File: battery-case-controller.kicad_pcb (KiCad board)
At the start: 6 copper layers, 109 x 55 mm, 187 parts, among them J31 +, J32 DISPLAY, J33 A, J34 HALL, J35 B, J36 MOT_AUX, J37 C, J38 CRANK, J39 GND, J40 CAN_IN, J41 CAN_OUT, J42 Debug, J43 SWD, M31 MountingHole_Pad, M32 MountingHole_Pad, M33 MountingHole_Pad, Q31 BSC040N08, Q32 BSC040N08, Q33 BSC040N08, Q34 BSC040N08, Q35 BSC040N08, Q36 BSC040N08, Q37 BSC040N08, Q38 BSC040N08, Q39 BSC040N08, Q40 BSC040N08, Q41 BSC040N08, Q42 BSC040N08, U31 Enable, U32 LM5109B, U33 INA240A2PWR, U34 LM5109B, U35 INA240A2PWR, U36 LM5109B, U37 INA240A2PWR, U38 LM5008, U39 XC6206P332MR, U40 XC6206P332MR, U41 LMR12010X, U42 SN65HVD230, U43 STM32G491CxT, X31 8MHz

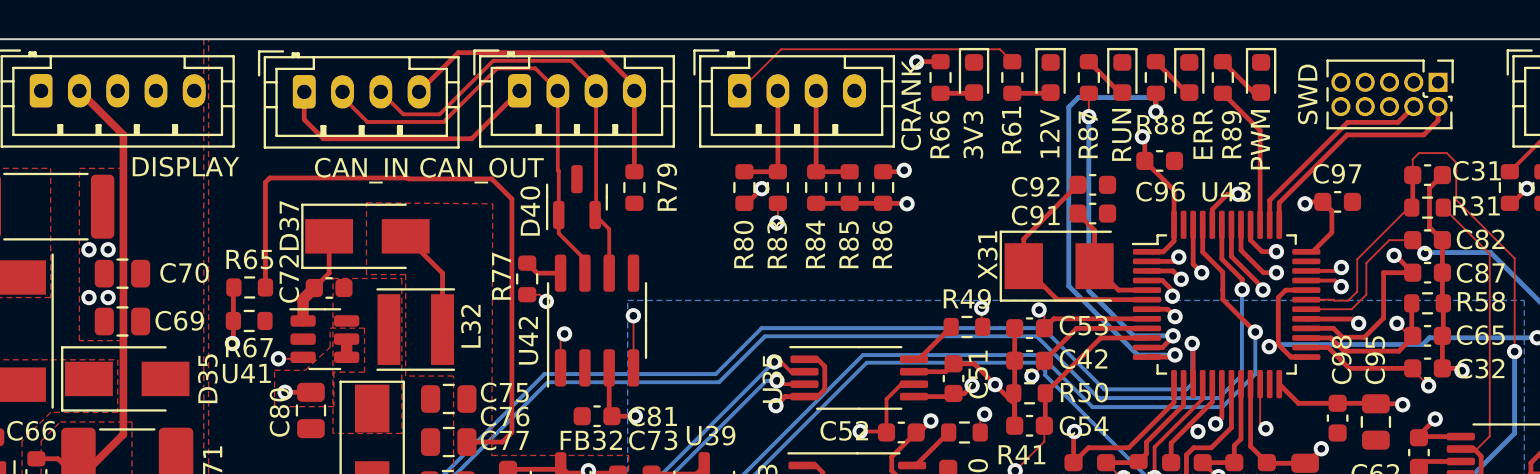
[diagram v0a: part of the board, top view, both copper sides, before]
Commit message: Fixed pinning error for Display RX and PWM Break
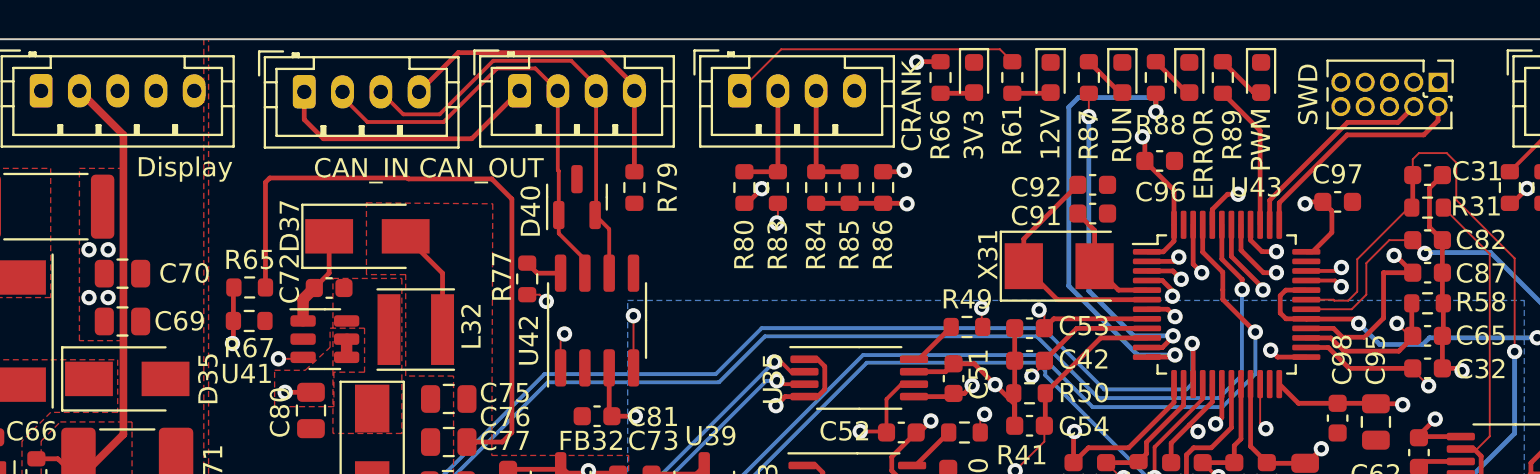
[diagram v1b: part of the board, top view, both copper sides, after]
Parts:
- D42: value ERR -> ERROR
- J32: value DISPLAY -> Display
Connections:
- U43 pad 25: /Interface/PWM_BREAK -> /mcu/DISP_RX
- U43 pad 29: /mcu/DISP_RX -> /Interface/PWM_BREAK
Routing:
- net /mcu/DISP_RX: track 74.1 -> 69.6 mm
- net /Interface/PWM_BREAK: track 27.7 -> 23.8 mm
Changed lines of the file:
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@@
   (net 99 "unconnected-(J43-Pad8)")
   (net 100 "unconnected-(J43-Pad9)")
-  (net 101 "Net-(U33-Pad8)")
+  (net 101 "Net-(R41-Pad1)")
   (net 102 "Net-(R43-Pad2)")
   (net 103 "Net-(R46-Pad2)")
-  (net 104 "Net-(U35-Pad8)")
+  (net 104 "Net-(R49-Pad1)")
   (net 105 "Net-(R51-Pad2)")
   (net 106 "Net-(R54-Pad2)")
-  (net 107 "Net-(U37-Pad8)")
+  (net 107 "Net-(R57-Pad1)")
   (net 108 "Net-(R59-Pad1)")
   (net 109 "Net-(R63-Pad2)")
@@
       (net 2 "GNDA") (pinfunction "REF1") (pintype "passive"))
     (pad "8" smd roundrect (at 2.8625 -0.975 180) (size 1.475 0.4) (layers "F.Cu" "F.Paste" "F.Mask") (roundrect_rratio 0.25)
-      (net 107 "Net-(U37-Pad8)") (pintype "output"))
+      (net 107 "Net-(R57-Pad1)") (pintype "output"))
     (model "${KICAD6_3DMODEL_DIR}/Package_SO.3dshapes/TSSOP-8_4.4x3mm_P0.65mm.wrl"
       (offset (xyz 0 0 0))
@@
       (effects (font (size 1 1) (thickness 0.15)))
     )
-    (fp_text value "DISPLAY" (at 7.5 4) (layer "F.SilkS")
+    (fp_text value "Display" (at 7.5 4) (layer "F.SilkS")
       (effects (font (size 1 1) (thickness 0.15)))
     )
@@
       (net 2 "GNDA") (pinfunction "REF1") (pintype "passive"))
     (pad "8" smd roundrect (at 2.8625 -0.975) (size 1.475 0.4) (layers "F.Cu" "F.Paste" "F.Mask") (roundrect_rratio 0.25)
-      (net 104 "Net-(U35-Pad8)") (pintype "output"))
+      (net 104 "Net-(R49-Pad1)") (pintype "output"))
     (model "${KICAD6_3DMODEL_DIR}/Package_SO.3dshapes/TSSOP-8_4.4x3mm_P0.65mm.wrl"
       (offset (xyz 0 0 0))
@@
     (fp_line (start -0.8 0.4125) (end -0.8 -0.4125) (layer "F.Fab") (width 0.1))
     (pad "1" smd roundrect (at -0.825 0) (size 0.8 0.95) (layers "F.Cu" "F.Paste" "F.Mask") (roundrect_rratio 0.25)
-      (net 104 "Net-(U35-Pad8)") (pintype "passive"))
+      (net 104 "Net-(R49-Pad1)") (pintype "passive"))
     (pad "2" smd roundrect (at 0.825 0) (size 0.8 0.95) (layers "F.Cu" "F.Paste" "F.Mask") (roundrect_rratio 0.25)
       (net 50 "/mcu/AIN_IA") (pintype "passive"))
@@
       (net 2 "GNDA") (pinfunction "REF1") (pintype "passive"))
     (pad "8" smd roundrect (at 2.8625 -0.975) (size 1.475 0.4) (layers "F.Cu" "F.Paste" "F.Mask") (roundrect_rratio 0.25)
-      (net 101 "Net-(U33-Pad8)") (pintype "output"))
+      (net 101 "Net-(R41-Pad1)") (pintype "output"))
     (model "${KICAD6_3DMODEL_DIR}/Package_SO.3dshapes/TSSOP-8_4.4x3mm_P0.65mm.wrl"
       (offset (xyz 0 0 0))
@@
     (fp_line (start -0.8 0.4125) (end -0.8 -0.4125) (layer "F.Fab") (width 0.1))
     (pad "1" smd roundrect (at -0.825 0) (size 0.8 0.95) (layers "F.Cu" "F.Paste" "F.Mask") (roundrect_rratio 0.25)
-      (net 101 "Net-(U33-Pad8)") (pintype "passive"))
+      (net 101 "Net-(R41-Pad1)") (pintype "passive"))
     (pad "2" smd roundrect (at 0.825 0) (size 0.8 0.95) (layers "F.Cu" "F.Paste" "F.Mask") (roundrect_rratio 0.25)
       (net 47 "/mcu/AIN_IB") (pintype "passive"))
@@
     (property "Sheetname" "mcu")
     (attr smd)
-    (fp_text reference "U43" (at 0 -5.85) (layer "F.SilkS")
+    (fp_text reference "U43" (at 1.55 -6.11) (layer "F.SilkS")
       (effects (font (size 1 1) (thickness 0.15)))
     )
@@
       (net 14 "+3V3") (pinfunction "VDD") (pintype "power_in"))
     (pad "25" smd roundrect (at 4.1625 2.75) (size 1.475 0.3) (layers "F.Cu" "F.Paste" "F.Mask") (roundrect_rratio 0.25)
-      (net 43 "/Interface/PWM_BREAK") (pinfunction "PB11") (pintype "bidirectional"))
+      (net 25 "/mcu/DISP_RX") (pinfunction "PB11") (pintype "bidirectional"))
     (pad "26" smd roundrect (at 4.1625 2.25) (size 1.475 0.3) (layers "F.Cu" "F.Paste" "F.Mask") (roundrect_rratio 0.25)
       (net 3 "/mcu/AIN_VDC") (pinfunction "PB12") (pintype "bidirectional"))
@@
       (net 18 "/Interface/TORQ_CRK") (pinfunction "PB14") (pintype "bidirectional"))
     (pad "29" smd roundrect (at 4.1625 0.75) (size 1.475 0.3) (layers "F.Cu" "F.Paste" "F.Mask") (roundrect_rratio 0.25)
-      (net 25 "/mcu/DISP_RX") (pinfunction "PB15") (pintype "bidirectional"))
+      (net 43 "/Interface/PWM_BREAK") (pinfunction "PB15") (pintype "bidirectional"))
     (pad "30" smd roundrect (at 4.1625 0.25) (size 1.475 0.3) (layers "F.Cu" "F.Paste" "F.Mask") (roundrect_rratio 0.25)
       (net 15 "/Interface/TEMP_MOT") (pinfunction "PA8") (pintype "bidirectional"))
@@
       (effects (font (size 1 1) (thickness 0.15)))
     )
-    (fp_text value "ERR" (at 3 -0.75 90) (layer "F.SilkS")
+    (fp_text value "ERROR" (at 4 -0.75 90) (layer "F.SilkS")
       (effects (font (size 1 1) (thickness 0.15)))
     )
@@
     (fp_line (start 0.8 0.4125) (end -0.8 0.4125) (layer "F.Fab") (width 0.1))
     (pad "1" smd roundrect (at -0.825 0 180) (size 0.8 0.95) (layers "F.Cu" "F.Paste" "F.Mask") (roundrect_rratio 0.25)
-      (net 107 "Net-(U37-Pad8)") (pintype "passive"))
+      (net 107 "Net-(R57-Pad1)") (pintype "passive"))
     (pad "2" smd roundrect (at 0.825 0 180) (size 0.8 0.95) (layers "F.Cu" "F.Paste" "F.Mask") (roundrect_rratio 0.25)
       (net 53 "/mcu/AIN_IC") (pintype "passive"))
@@
   (segment (start 172.2 96.9) (end 173.75 95.35) (width 0.1) (layer "In4.Cu") (net 24))
   (segment (start 115.75 77.7) (end 134.95 96.9) (width 0.1) (layer "In4.Cu") (net 24))
-  (segment (start 178.372937 89.622937) (end 178.6 89.85) (width 0.25) (layer "F.Cu") (net 25))
-  (segment (start 175.8625 89.61) (end 175.875437 89.622937) (width 0.25) (layer "F.Cu") (net 25))
-  (segment (start 175.875437 89.622937) (end 178.372937 89.622937) (width 0.25) (layer "F.Cu") (net 25))
-  (via (at 178.6 89.85) (size 0.8) (drill 0.4) (layers "F.Cu" "B.Cu") (net 25))
+  (segment (start 174.36 91.61) (end 174 91.25) (width 0.25) (layer "F.Cu") (net 25))
+  (segment (start 175.8625 91.61) (end 174.36 91.61) (width 0.25) (layer "F.Cu") (net 25))
+  (via (at 174 91.25) (size 0.8) (drill 0.4) (layers "F.Cu" "B.Cu") (net 25))
   (segment (start 136.35 96.3) (end 171.6 96.3) (width 0.1) (layer "In4.Cu") (net 25))
-  (segment (start 178.05 89.85) (end 178.6 89.85) (width 0.1) (layer "In4.Cu") (net 25))
   (segment (start 117.75 77.7) (end 136.35 96.3) (width 0.1) (layer "In4.Cu") (net 25))
-  (segment (start 171.6 96.3) (end 178.05 89.85) (width 0.1) (layer "In4.Cu") (net 25))
+  (segment (start 171.6 96.3) (end 174 93.9) (width 0.1) (layer "In4.Cu") (net 25))
+  (segment (start 174 93.9) (end 174 91.25) (width 0.1) (layer "In4.Cu") (net 25))
   (segment (start 163 107.7) (end 159.875 104.575) (width 0.25) (layer "F.Cu") (net 26))
   (segment (start 159.875 104.575) (end 159.75 104.575) (width 0.25) (layer "F.Cu") (net 26))
@@
   (segment (start 188.25 81.925) (end 188.25 81.75) (width 0.2) (layer "F.Cu") (net 42))
   (segment (start 188.25 81.75) (end 190.75 79.25) (width 0.2) (layer "F.Cu") (net 42))
-  (segment (start 174.4 88.5) (end 174.79 88.11) (width 0.25) (layer "F.Cu") (net 43))
-  (segment (start 174.4 90.950685) (end 174.039479 90.950685) (width 0.25) (layer "F.Cu") (net 43))
-  (segment (start 174.4 90.950685) (end 174.4 88.5) (width 0.25) (layer "F.Cu") (net 43))
-  (segment (start 175.8625 91.61) (end 175.059315 91.61) (width 0.25) (layer "F.Cu") (net 43))
-  (segment (start 175.059315 91.61) (end 174.4 90.950685) (width 0.25) (layer "F.Cu") (net 43))
+  (segment (start 178.372937 89.622937) (end 178.6 89.85) (width 0.25) (layer "F.Cu") (net 43))
+  (segment (start 175.8625 89.61) (end 175.875437 89.622937) (width 0.25) (layer "F.Cu") (net 43))
+  (segment (start 174.5 89.305) (end 174.5 88.4) (width 0.25) (layer "F.Cu") (net 43))
+  (segment (start 175.8625 89.61) (end 174.805 89.61) (width 0.25) (layer "F.Cu") (net 43))
+  (segment (start 174.5 88.4) (end 174.79 88.11) (width 0.25) (layer "F.Cu") (net 43))
   (segment (start 188.25 90.2755) (end 187.9255 90.6) (width 0.25) (layer "F.Cu") (net 43))
+  (segment (start 175.875437 89.622937) (end 178.372937 89.622937) (width 0.25) (layer "F.Cu") (net 43))
   (segment (start 174.79 88.11) (end 175.8625 88.11) (width 0.25) (layer "F.Cu") (net 43))
-  (segment (start 174.039479 90.950685) (end 173.9245 91.065664) (width 0.25) (layer "F.Cu") (net 43))
   (segment (start 188.25 83.575) (end 188.25 90.2755) (width 0.25) (layer "F.Cu") (net 43))
-  (via (at 173.9245 91.065664) (size 0.8) (drill 0.4) (layers "F.Cu" "B.Cu") (net 43))
+  (segment (start 174.805 89.61) (end 174.5 89.305) (width 0.25) (layer "F.Cu") (net 43))
   (via (at 187.9255 90.6) (size 0.8) (drill 0.4) (layers "F.Cu" "B.Cu") (net 43))
+  (via (at 178.6 89.85) (size 0.8) (drill 0.4) (layers "F.Cu" "B.Cu") (net 43))
+  (segment (start 179.7 90.95) (end 178.6 89.85) (width 0.25) (layer "B.Cu") (net 43))
   (segment (start 182.3 90.6) (end 187.9255 90.6) (width 0.25) (layer "B.Cu") (net 43))
-  (segment (start 173.9245 91.065664) (end 174.040164 90.95) (width 0.25) (layer "B.Cu") (net 43))
+  (segment (start 179.7 90.95) (end 181.95 90.95) (width 0.25) (layer "B.Cu") (net 43))
   (segment (start 181.95 90.95) (end 182.3 90.6) (width 0.25) (layer "B.Cu") (net 43))
-  (segment (start 174.040164 90.95) (end 181.95 90.95) (width 0.25) (layer "B.Cu") (net 43))
   (segment (start 170.95 84.6975) (end 170.95 83.894315) (width 0.25) (layer "F.Cu") (net 44))
   (segment (start 135.8 88.35) (end 136.15 88.7) (width 0.1) (layer "F.Cu") (net 44))

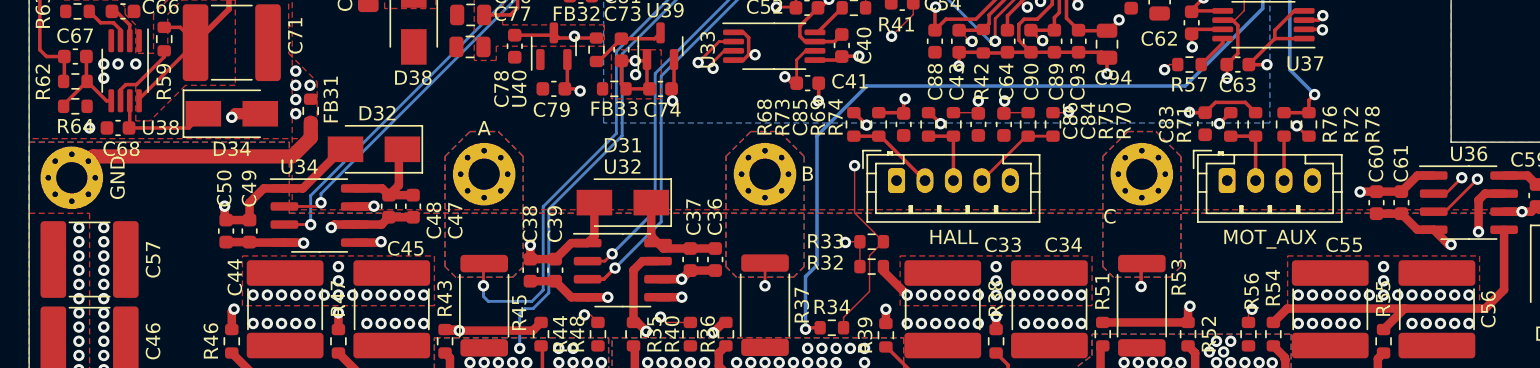
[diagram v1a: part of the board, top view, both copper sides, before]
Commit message: added Pulldowns to the PWM wires
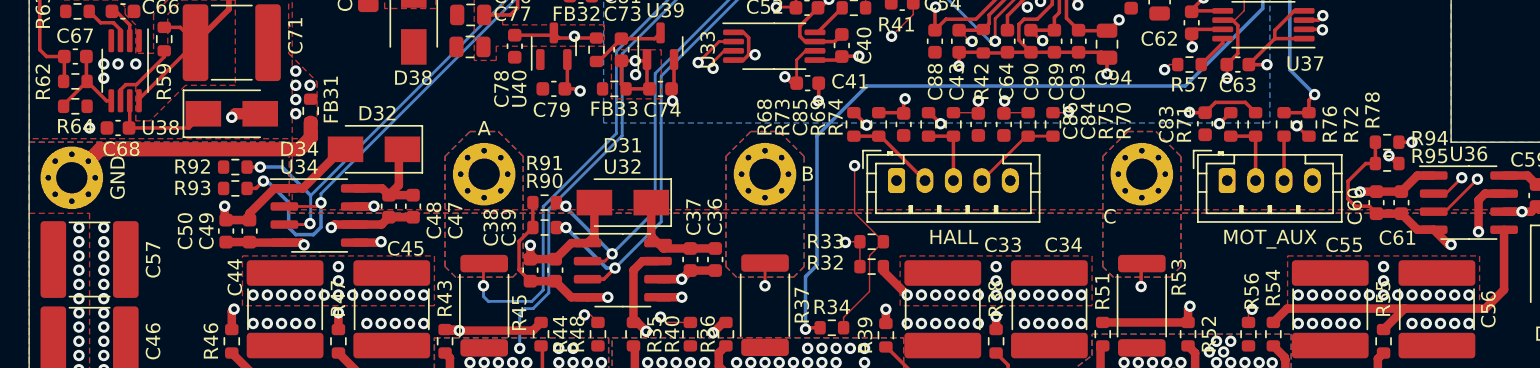
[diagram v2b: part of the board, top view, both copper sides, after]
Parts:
- added R90: 10k, Resistor_SMD:R_0603_1608Metric, F.Cu at (136.2, 111.0)
- added R91: 10k, Resistor_SMD:R_0603_1608Metric, F.Cu at (136.2, 109.2)
- added R92: 10k, Resistor_SMD:R_0603_1608Metric, F.Cu at (114.5, 106.8)
- added R93: 10k, Resistor_SMD:R_0603_1608Metric, F.Cu at (114.5, 108.2)
- added R94: 10k, Resistor_SMD:R_0603_1608Metric, F.Cu at (195.5, 105.0)
- added R95: 10k, Resistor_SMD:R_0603_1608Metric, F.Cu at (195.5, 106.5)
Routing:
- net GNDPWR: track 80.7 -> 94.8 mm
- net /mcu/PWM_A: track 72.9 -> 82.9 mm, vias 2 -> 3
- net /mcu/PWM_B: track 59.4 -> 64.9 mm, vias 2 -> 3
- net /mcu/PWM_BN: track 52.6 -> 57.9 mm, vias 2 -> 3
- net /mcu/PWM_AN: track 67.4 -> 72.6 mm, vias 2 -> 3
- net /mcu/PWM_CN: track 50.5 -> 52.6 mm, vias 2 -> 3
- net /mcu/PWM_C: track 50.9 -> 52.5 mm, vias 2 -> 3
